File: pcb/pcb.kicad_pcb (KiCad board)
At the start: 2 copper layers, 65 x 45 mm, 42 parts, among them J1 Temp +, J2 Temp -, J3 KNX, J4 Screw_Terminal_01x02, J5 Screw_Terminal_01x02, J6 Common, SW1 SW_Push_Dual, U1 STM32F072C8Tx, U2 MAX31865, U3 LM7805, U4 AMS1117

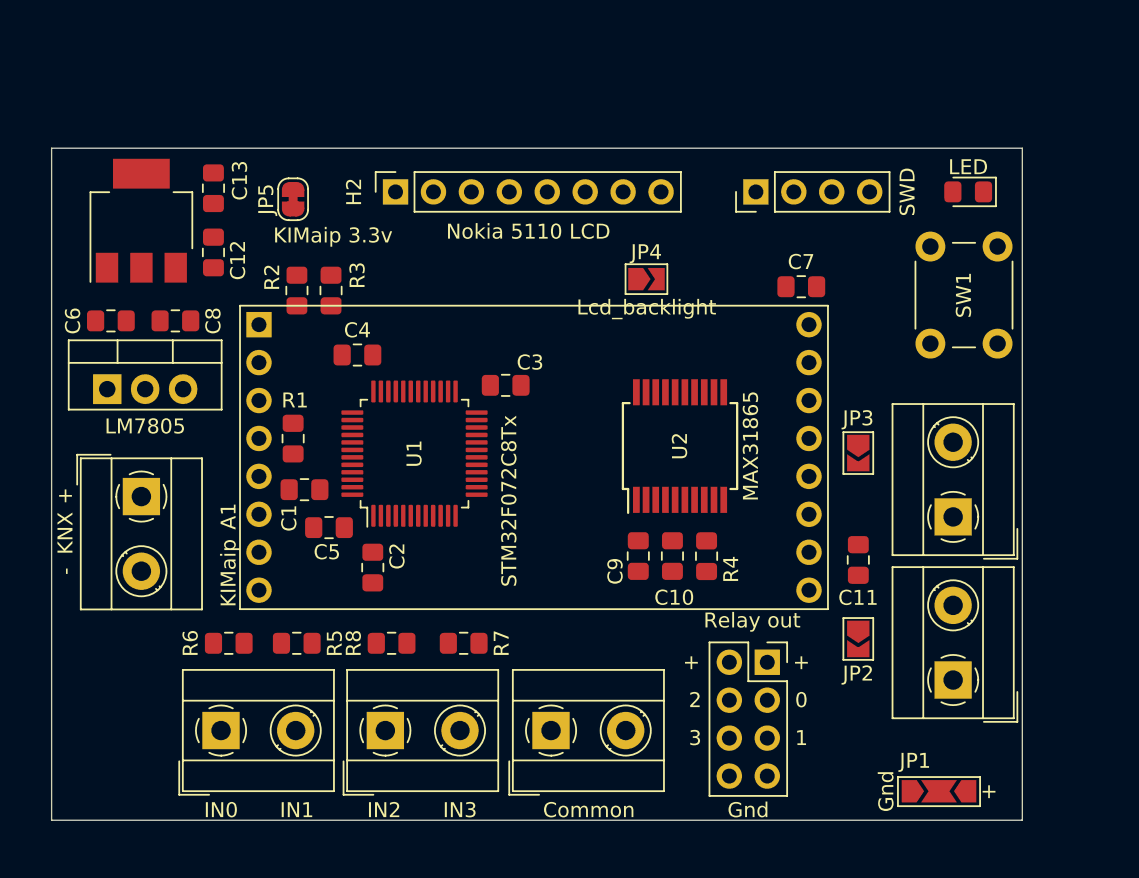
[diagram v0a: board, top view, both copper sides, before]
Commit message: pcb routed
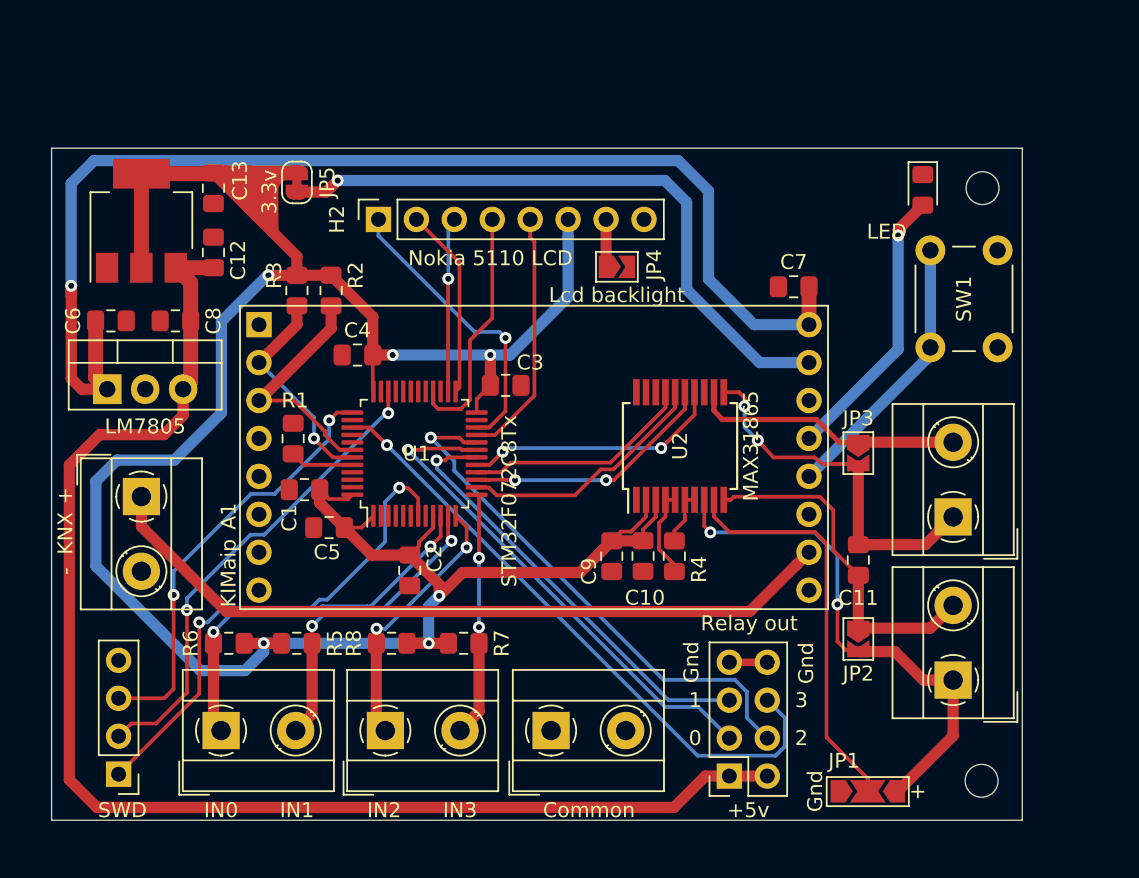
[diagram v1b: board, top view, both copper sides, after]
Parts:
- added REF**: MountingHole_2.2mm_M2, MountingHole:MountingHole_2.2mm_M2, F.Cu at (152.3, 82.4)
- added REF**: MountingHole_2.2mm_M2, MountingHole:MountingHole_2.2mm_M2, F.Cu at (152.3, 42.7)
- JP4: value Lcd_backlight -> Lcd backlight
- JP5: value KIMaip 3.3v -> 3.3v
- moved H1 57.8 mm to (94.5, 81.9), turned to 180 degrees
- moved H3 8.03 mm to (135.4, 82.0), turned to 180 degrees
- moved JP1 4.77 mm to (144.7, 83.1)
- moved D1 3.04 mm to (148.3, 42.8), turned to 270 degrees
- moved C2 2.48 mm to (114.0, 68.3)
- moved R2 2.29 mm to (108.7, 49.5)
- moved R3 2.29 mm to (106.4, 49.5)
- moved H2 2.17 mm to (111.9, 44.8)
- moved R4 2.16 mm to (131.7, 67.3)
- moved JP4 2.14 mm to (127.9, 47.9)
- moved C10 1.97 mm to (129.6, 67.3)
- moved C9 1.78 mm to (127.5, 67.3)
- moved JP5 1.16 mm to (106.4, 42.3), turned to 270 degrees
- moved C7 0.51 mm to (139.7, 49.3)
- moved SW1 0.25 mm to (148.8, 53.3)
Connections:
- U1 pad 18: /OUT_0 -> /OUT_1
- U1 pad 19: /OUT_1 -> /OUT_0
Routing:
- net +3V3: track 0.00 -> 188.9 mm, vias 0 -> 6
- net +5V: track 0.00 -> 91.5 mm
- net +12V: track 0.00 -> 82.0 mm, vias 0 -> 1
- net Net-(A1-Pad10): track 0.00 -> 50.7 mm
- net Net-(A1-Pad15): track 0.00 -> 43.2 mm, vias 0 -> 1
- net /OUT_3: track 0.00 -> 41.9 mm, vias 0 -> 1
- net /OUT_2: track 0.00 -> 35.5 mm, vias 0 -> 1
- net Net-(J1-Pad1): track 0.00 -> 35.0 mm, vias 0 -> 2
- net /OUT_0: track 0.00 -> 34.2 mm, vias 0 -> 1
- net /NRST: track 0.00 -> 33.8 mm, vias 0 -> 2
- net /SWDIO: track 0.00 -> 32.2 mm, vias 0 -> 2
- net /OUT_1: track 0.00 -> 29.3 mm, vias 0 -> 1
- net /SWDCLK: track 0.00 -> 28.9 mm, vias 0 -> 2
- net Net-(JP1-Pad2): track 0.00 -> 27.1 mm
- net /BIN_0: track 0.00 -> 26.1 mm, vias 0 -> 2
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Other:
- board text added: "+5v"

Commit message: pcb klaar
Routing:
- net GND: track 2.54 -> 28.1 mm, vias 0 -> 9
- net /LCD_CLK: track 16.9 -> 19.8 mm
- added copper zone on B.Cu, net GND
- added copper zone on F.Cu, net GND
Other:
- board text added: "KNX temperature monitor V1.0 (2019)"
- board text added: "Olivier Van den Eede"
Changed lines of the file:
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@@
   (general
     (thickness 1.6)
-    (drawings 19)
-    (tracks 435)
+    (drawings 21)
+    (tracks 467)
     (zones 0)
     (modules 44)
@@
     (last_trace_width 0.25)
     (trace_clearance 0.2)
-    (zone_clearance 0.508)
+    (zone_clearance 0.4)
     (zone_45_only no)
     (trace_min 0.2)
@@
       (effects (font (size 1 1) (thickness 0.15)))
     )
-    (fp_text value "Temp +" (at -3.81 0.508 180) (layer F.Fab)
+    (fp_text value "Temp +" (at -3.81 0.508 180) (layer F.SilkS)
       (effects (font (size 1 1) (thickness 0.15)))
     )
@@
       (effects (font (size 1 1) (thickness 0.15)))
     )
-    (fp_text value "Temp -" (at 8.89 0.508) (layer F.Fab)
+    (fp_text value "Temp -" (at 8.89 0.508) (layer F.SilkS)
       (effects (font (size 1 1) (thickness 0.15)))
     )
@@
       (effects (font (size 1 1) (thickness 0.15)))
     )
-    (fp_text value AMS1117 (at -0.102 -4.318 90) (layer F.Fab)
+    (fp_text value AMS1117 (at -0.102 -4.318 90) (layer F.SilkS)
       (effects (font (size 1 1) (thickness 0.15)))
     )
@@
       (rotate (xyz 0 0 0))
     )
+  )
+  (gr_text "KNX temperature\nmonitor V1.0 (2019)" (at 139.2428 42.2402) (layer F.SilkS)
+    (effects (font (size 1 1) (thickness 0.15)))
+  )
+  (gr_text "Olivier Van den Eede" (at 121.7676 41.6814) (layer F.SilkS)
+    (effects (font (size 1 1) (thickness 0.15)))
   )
   (gr_text - (at 90.932 68.326 90) (layer F.SilkS)
@@
   (segment (start 91.313 49.2125) (end 91.313 55.4235) (width 0.75) (layer F.Cu) (net 10))
   (segment (start 135.382 74.422) (end 137.922 74.422) (width 0.5) (layer F.Cu) (net 4))
+  (via (at 129.5908 69.8754) (size 0.8) (drill 0.4) (layers F.Cu B.Cu) (net 4))
+  (via (at 127.4826 69.8754) (size 0.8) (drill 0.4) (layers F.Cu B.Cu) (net 4))
+  (via (at 129.6416 72.1868) (size 0.8) (drill 0.4) (layers F.Cu B.Cu) (net 4))
+  (via (at 105.8672 65.4304) (size 0.8) (drill 0.4) (layers F.Cu B.Cu) (net 4))
+  (segment (start 105.8672 65.4304) (end 108.5596 65.4304) (width 0.75) (layer B.Cu) (net 4))
+  (segment (start 112.2172 61.7728) (end 112.2172 61.7728) (width 0.75) (layer B.Cu) (net 4))
+  (via (at 112.2172 61.7728) (size 0.8) (drill 0.4) (layers F.Cu B.Cu) (net 4))
+  (segment (start 111.288 62.702) (end 110.1375 62.702) (width 0.25) (layer F.Cu) (net 4))
+  (segment (start 112.2172 61.7728) (end 111.288 62.702) (width 0.25) (layer F.Cu) (net 4))
+  (segment (start 112.2172 61.7728) (end 113.8936 61.7728) (width 0.25) (layer F.Cu) (net 4))
+  (segment (start 115.05 62.9292) (end 115.05 64.6145) (width 0.25) (layer F.Cu) (net 4))
+  (segment (start 113.8936 61.7728) (end 115.05 62.9292) (width 0.25) (layer F.Cu) (net 4))
+  (via (at 109.5248 55.88) (size 0.8) (drill 0.4) (layers F.Cu B.Cu) (net 4))
+  (via (at 114.0206 54.9148) (size 0.8) (drill 0.4) (layers F.Cu B.Cu) (net 4))
+  (segment (start 112.05 55.452) (end 112.05 56.2895) (width 0.25) (layer F.Cu) (net 4))
+  (segment (start 112.5872 54.9148) (end 112.05 55.452) (width 0.25) (layer F.Cu) (net 4))
+  (segment (start 114.0206 54.9148) (end 112.5872 54.9148) (width 0.25) (layer F.Cu) (net 4))
+  (via (at 121.412 58.039) (size 0.8) (drill 0.4) (layers F.Cu B.Cu) (net 4))
+  (segment (start 121.43 58.021) (end 121.412 58.039) (width 0.25) (layer F.Cu) (net 4))
+  (segment (start 121.43 55.88) (end 121.43 58.021) (width 0.25) (layer F.Cu) (net 4))
+  (via (at 114.2238 58.1914) (size 0.8) (drill 0.4) (layers F.Cu B.Cu) (net 4))
+  (segment (start 118.4519 58.1914) (end 118.4625 58.202) (width 0.25) (layer F.Cu) (net 4))
+  (segment (start 114.2238 58.1914) (end 118.4519 58.1914) (width 0.25) (layer F.Cu) (net 4))
+  (segment (start 129.805 55.219) (end 129.794 55.208) (width 0.25) (layer F.Cu) (net 4))
+  (segment (start 129.805 56.344) (end 129.805 55.219) (width 0.25) (layer F.Cu) (net 4))
+  (segment (start 129.805 56.344) (end 130.455 56.344) (width 0.25) (layer F.Cu) (net 4))
+  (segment (start 130.455 55.219) (end 130.4544 55.2184) (width 0.25) (layer F.Cu) (net 4))
+  (segment (start 130.455 56.344) (end 130.455 55.219) (width 0.25) (layer F.Cu) (net 4))
+  (segment (start 130.4544 55.2184) (end 130.4544 54.483) (width 0.25) (layer F.Cu) (net 4))
+  (segment (start 129.805 57.469) (end 128.9304 58.3436) (width 0.25) (layer F.Cu) (net 4))
+  (segment (start 129.805 57.469) (end 129.805 56.344) (width 0.25) (layer F.Cu) (net 4))
   (segment (start 128.131372 65.670628) (end 127.508 66.294) (width 0.25) (layer F.Cu) (net 9))
   (segment (start 128.803372 65.670628) (end 128.131372 65.670628) (width 0.25) (layer F.Cu) (net 9))
@@
   (segment (start 119.507 51.3715) (end 119.507 44.7675) (width 0.25) (layer F.Cu) (net 20))
   (segment (start 118.01249 52.86601) (end 119.507 51.3715) (width 0.25) (layer F.Cu) (net 20))
-  (segment (start 122.047 45.969581) (end 122.047 44.7675) (width 0.25) (layer F.Cu) (net 21))
-  (segment (start 122.33001 46.252591) (end 122.047 45.969581) (width 0.25) (layer F.Cu) (net 21))
-  (segment (start 122.33001 56.56818) (end 122.33001 46.252591) (width 0.25) (layer F.Cu) (net 21))
-  (segment (start 119.69619 59.202) (end 122.33001 56.56818) (width 0.25) (layer F.Cu) (net 21))
-  (segment (start 118.4625 59.202) (end 119.69619 59.202) (width 0.25) (layer F.Cu) (net 21))
+  (segment (start 124.206 46.9265) (end 122.047 44.7675) (width 0.25) (layer F.Cu) (net 21))
+  (segment (start 124.206 56.9468) (end 124.206 46.9265) (width 0.25) (layer F.Cu) (net 21))
+  (segment (start 118.4625 59.202) (end 121.9508 59.202) (width 0.25) (layer F.Cu) (net 21))
+  (segment (start 121.9508 59.202) (end 124.206 56.9468) (width 0.25) (layer F.Cu) (net 21))
   (segment (start 127.127 44.7675) (end 127.127 47.9425) (width 0.75) (layer F.Cu) (net 22))
   (via (at 115.7732 60.9092) (size 0.8) (drill 0.4) (layers F.Cu B.Cu) (net 23))
@@
   (segment (start 135.756003 75.597001) (end 130.969001 75.597001) (width 0.25) (layer B.Cu) (net 25))
   (segment (start 130.969001 75.597001) (end 116.967 61.595) (width 0.25) (layer B.Cu) (net 25))
-  (via (at 112.4585 59.8805) (size 0.8) (drill 0.4) (layers F.Cu B.Cu) (net 26))
   (segment (start 139.097001 78.137001) (end 139.097001 80.066001) (width 0.25) (layer B.Cu) (net 26))
   (segment (start 137.922 76.962) (end 139.097001 78.137001) (width 0.25) (layer B.Cu) (net 26))
@@
   (segment (start 133.261499 80.677001) (end 112.4585 59.874002) (width 0.25) (layer B.Cu) (net 26))
   (segment (start 111.28 58.702) (end 110.1375 58.702) (width 0.25) (layer F.Cu) (net 26))
-  (segment (start 112.4585 59.8805) (end 111.28 58.702) (width 0.25) (layer F.Cu) (net 26))
+  (via (at 111.9124 59.3344) (size 0.8) (drill 0.4) (layers F.Cu B.Cu) (net 26))
+  (segment (start 112.4585 59.874002) (end 112.452002 59.874002) (width 0.25) (layer B.Cu) (net 26))
+  (segment (start 112.452002 59.874002) (end 111.9124 59.3344) (width 0.25) (layer B.Cu) (net 26))
+  (segment (start 111.9124 59.3344) (end 111.28 58.702) (width 0.25) (layer F.Cu) (net 26))
   (segment (start 150.368 79.343) (end 146.653 83.058) (width 0.75) (layer F.Cu) (net 27))
   (segment (start 150.368 75.612) (end 150.368 79.343) (width 0.75) (layer F.Cu) (net 27))
@@
   (segment (start 137.414 54.356) (end 140.716 54.356) (width 0.75) (layer B.Cu) (net 58))
   (segment (start 132.5245 49.4665) (end 137.414 54.356) (width 0.75) (layer B.Cu) (net 58))
+  (zone (net 4) (net_name GND) (layer B.Cu) (hatch edge 0.508)
+    (connect_pads (clearance 0.4))
+    (min_thickness 0.254)
+    (fill yes (arc_segments 32) (thermal_gap 0.508) (thermal_bridge_width 0.508))
+    (polygon
+      (pts
+        (xy 89.2048 39.3446) (xy 155.7782 39.3446) (xy 155.6512 86.7156) (xy 89.1032 86.5886)
+      )
+    )
+  )
+  (zone (net 4) (net_name GND) (layer F.Cu) (hatch edge 0.508)
+    (connect_pads (clearance 0.25))
+    (min_thickness 0.254)
+    (fill yes (arc_segments 32) (thermal_gap 0.508) (thermal_bridge_width 0.508))
+    (polygon
+      (pts
+        (xy 89.154 39.37) (xy 155.829 39.3954) (xy 155.8798 86.8172) (xy 88.9254 86.5886)
+      )
+    )
+  )
 )

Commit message: pcb ordered
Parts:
- moved R5 0.74 mm to (106.4, 73.9)
- moved R8 0.74 mm to (112.7, 73.9)
- moved R7 0.74 mm to (117.6, 73.9)
- moved R6 0.74 mm to (101.9, 73.9)
- moved J6 0.51 mm to (123.4, 79.5)
- moved J5 0.51 mm to (112.3, 79.5)
- moved J4 0.51 mm to (101.3, 79.5)
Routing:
- net GND: track 28.1 -> 74.6 mm, vias 9 -> 11
- net /SWDCLK: track 28.9 -> 27.1 mm
- net /LCD_CLK: track 19.8 -> 18.4 mm
- net /BIN_2: track 17.9 -> 18.9 mm
- net /SWDIO: track 32.2 -> 31.2 mm
- net /BIN_0: track 26.1 -> 27.0 mm
- net Net-(A1-Pad10): track 50.7 -> 49.8 mm
- net /NRST: track 33.8 -> 33.2 mm
- net /BIN_3: track 16.4 -> 16.9 mm
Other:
- board text added: "Rst"

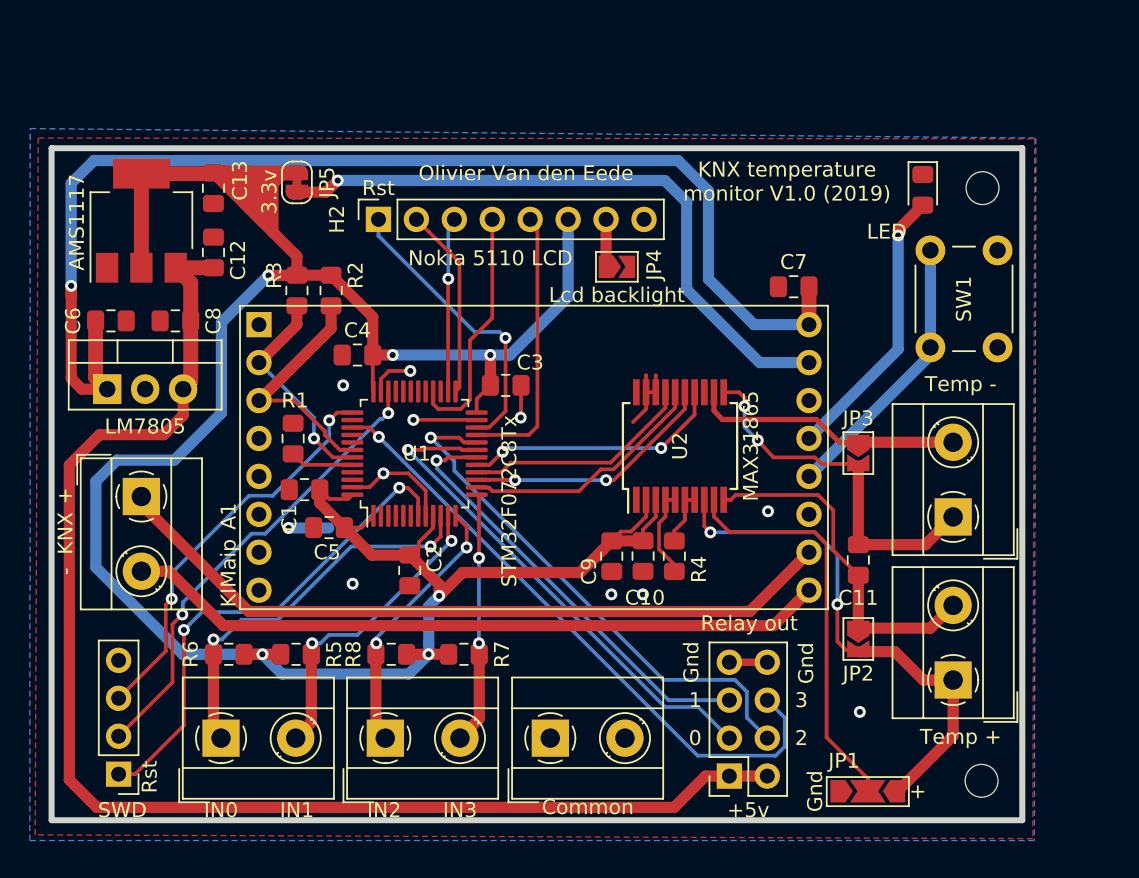
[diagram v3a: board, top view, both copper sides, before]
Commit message: add rdry trace to pcb
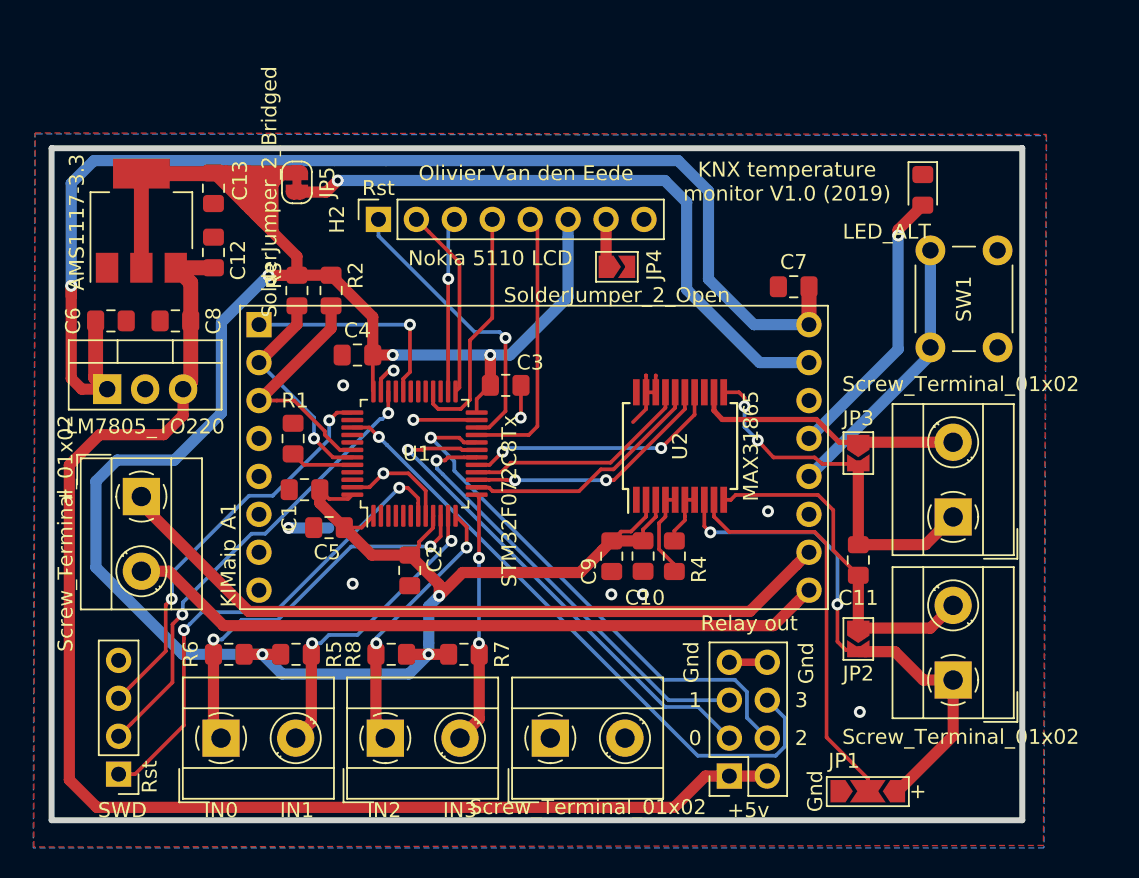
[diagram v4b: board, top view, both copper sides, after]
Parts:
- removed REF** (x2): MountingHole_2.2mm_M2, MountingHole:MountingHole_2.2mm_M2
- D1: value LED -> LED_ALT
- J1: value Temp + -> Screw_Terminal_01x02
- J2: value Temp - -> Screw_Terminal_01x02
- J3: value KNX -> Screw_Terminal_01x02
- J6: value Common -> Screw_Terminal_01x02
- JP4: value Lcd backlight -> SolderJumper_2_Open
- JP5: value 3.3v -> SolderJumper_2_Bridged
- U3: value LM7805 -> LM7805_TO220
- U4: value AMS1117 -> AMS1117-3.3
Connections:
- A1 pad 1: Net-(A1-Pad1) -> /DRDY
- U1 pad 32: Net-(U1-Pad32) -> /DRDY
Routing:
- net /DRDY: track 0.00 -> 14.8 mm, vias 0 -> 1
